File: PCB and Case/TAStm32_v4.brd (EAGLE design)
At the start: 50 x 100 mm, 37 parts, among them J1 ZX62D-B-5PA8, J10 RJSSE538002, J11 RJSSE538002, J12 SOICBITE, J13 CONSOLE_RESET, J2 UE27-AC54-100, J3 OLED128X64, J4 CONSOLE_RESET, J5 95278-802A12LF, J6 SAMTEC-TSM-106-01-X-SV_SAMTEC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, J7 SAMTEC-TSM-106-01-X-SV_SAMTEC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, J8 SAMTEC-TSM-106-01-X-SV_SAMTEC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, J9 SAMTEC-TSM-106-01-X-SV_SAMTEC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, U1 STM32F446RET6, U2 3.3V REG, Y1 8MHz

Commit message: 3D stuff
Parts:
- J10, J11: value RJSSE538002 -> RJSSE538002_RJSSE538002; device RJSSE538002:AMPHENOL_RJSSE538002 -> TAStm32_v4:AMPHENOL_RJSSE538002
- J13, J4: device TAStm32_v4:SAMTEC-TSM-102-01-X-SH_SAMTEC-TSM-102-01-X-SH -> TAStm32_v4:SAMTEC-TSM-102-01-X-SH
- J6, J7, J8, J9: value SAMTEC-TSM-106-01-X-SV_SAMTEC-TSM-106-01-X-SVJ -> SAMTEC-TSM-106-01-X-SV_SAMTEC-TSM-106-01-X-SV; device TAStm32_v4:SAMTEC-TSM-106-01-X-SV_SAMTEC-TSM-106-01-X-SV -> TAStm32_v4:SAMTEC-TSM-106-01-X-SV
- Y1: device TAStm32_v4:ABMM-8.000MHZ-B2-T_DFN-4 -> TAStm32_v4:DFN-4

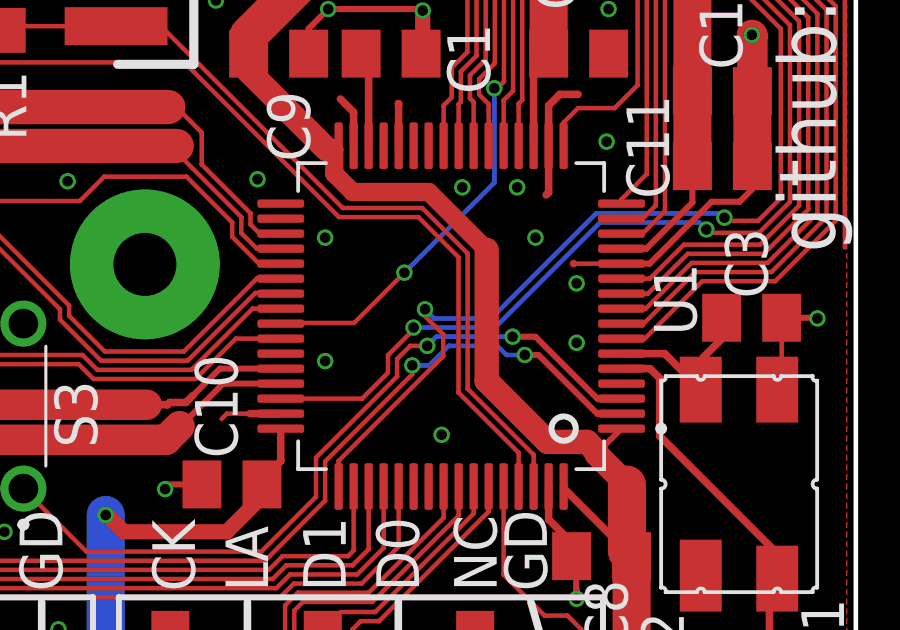
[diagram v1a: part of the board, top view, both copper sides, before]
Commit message: 3D packages
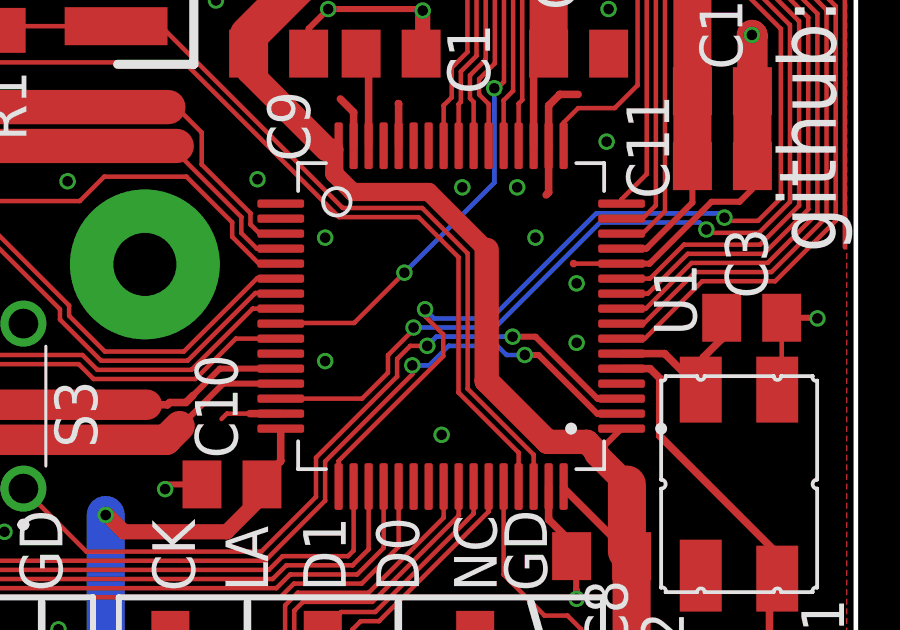
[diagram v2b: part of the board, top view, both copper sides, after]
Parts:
- U1: device TAStm32_v4:STM32F446RET6_QFP50P1200X1200X160-64N -> STM32F446RET6:QFP50P1200X1200X160-64N
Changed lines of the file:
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@@
 </layers>
 <board>
-<fusionsync huburn="a.cGVyc29uYWw6dWUyZjk5ODBk" projecturn="a.cGVyc29uYWw6dWUyZGI3NDIzIzIwMjAwNDAyMjgyMjQ0MjAx" f3durn="urn:adsk.wipprod:dm.lineage:3hYDGigSRSyFbyUFu3cILQ" pcbguid="358a8c1f-667c-482f-bf1c-2fc096c4186a" lastpulledtime="" lastsyncedchangeguid="38c33caf-a1b4-3c75-6ae5-50c6f9a0fab9"/>
+<fusionsync huburn="a.cGVyc29uYWw6dWUyZjk5ODBk" projecturn="a.cGVyc29uYWw6dWUyZGI3NDIzIzIwMjAwNDAyMjgyMjQ0MjAx" f3durn="urn:adsk.wipprod:dm.lineage:3hYDGigSRSyFbyUFu3cILQ" pcbguid="358a8c1f-667c-482f-bf1c-2fc096c4186a" lastpulledtime="" lastsyncedchangeguid="3421df81-c885-fb27-6cc6-82ec7bf5822e"/>
 <plain>
 <wire x1="0" y1="3" x2="0" y2="97" width="0.1524" layer="20"/>
@@
 <attribute name="VALUE" x="46.5508" y="45.9" size="1.016" layer="27" rot="R180"/>
 </element>
-<element name="U1" library="TAStm32_v4" package="STM32F446RET6_QFP50P1200X1200X160-64N" value="STM32F446RET6" x="36.508" y="36.5" smashed="yes" rot="R180">
-<attribute name="DESCRIPTION" value=" MCU 32-Bit STM32 ARM Cortex M4 RISC 512KB Flash 2.5V/3.3V 64-Pin LQFP Tray " x="36.508" y="36.5" size="1.778" layer="27" rot="R180" display="off"/>
-<attribute name="DIGI-KEY_PART_NUMBER" value="" x="36.508" y="36.5" size="1.778" layer="27" rot="R180" display="off"/>
-<attribute name="DIGI-KEY_PURCHASE_URL" value="" x="36.508" y="36.5" size="1.778" layer="27" rot="R180" display="off"/>
-<attribute name="MF" value="STMicroelectronics" x="36.508" y="36.5" size="1.778" layer="27" rot="R180" display="off"/>
-<attribute name="MP" value="STM32F446RET6" x="36.508" y="36.5" size="1.778" layer="27" rot="R180" display="off"/>
+<element name="U1" library="STM32F446RET6" package="QFP50P1200X1200X160-64N" package3d_urn="urn:adsk.eagle:package:18856813/2" value="STM32F446RET6" x="36.508" y="36.5" smashed="yes" rot="R180">
 <attribute name="NAME" x="43.26733125" y="38.258659375" size="1.4224" layer="25" font="vector" ratio="15" rot="R270"/>
-<attribute name="PACKAGE" value="LQFP-64 STMicroelectronics" x="36.508" y="36.5" size="1.778" layer="27" rot="R180" display="off"/>
 <attribute name="VALUE" x="43.0162" y="45.01071875" size="1.2716" layer="27" rot="R180"/>
 </element>

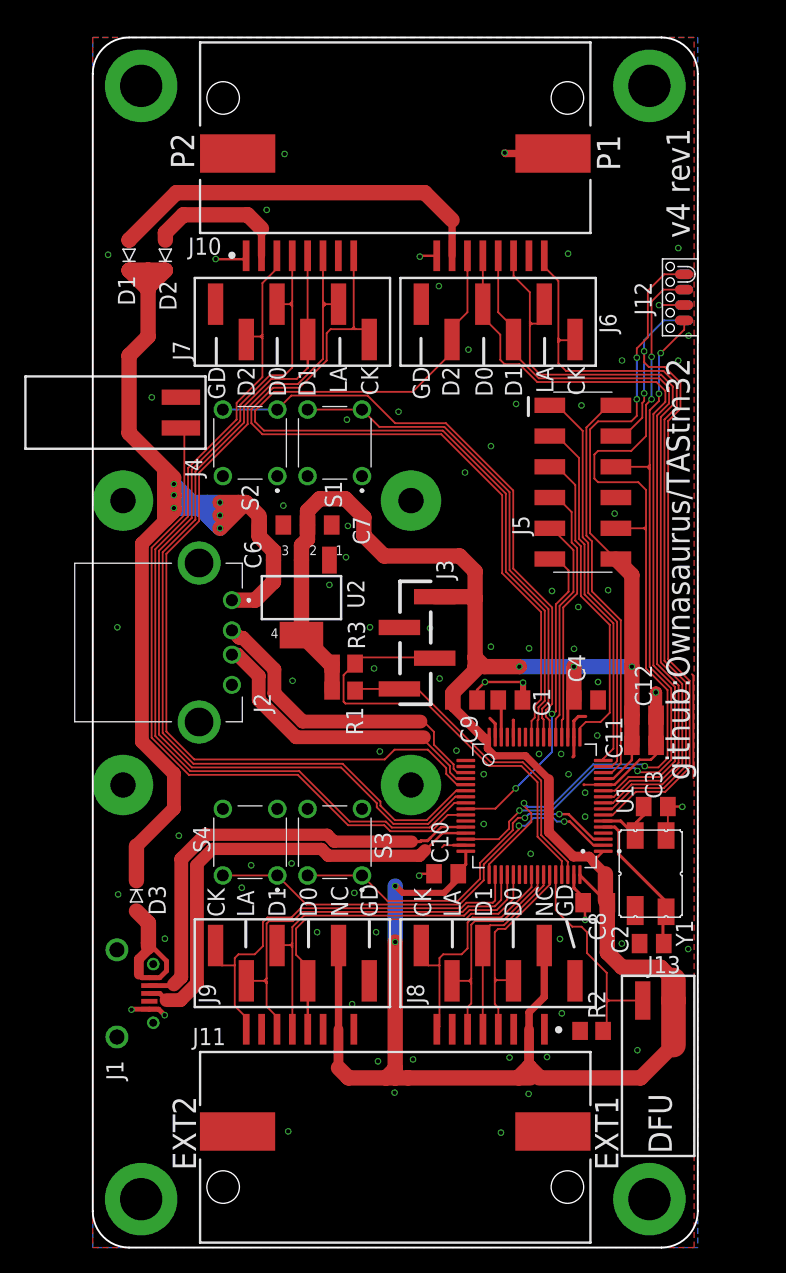
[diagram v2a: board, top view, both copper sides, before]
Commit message: Started adding level translators
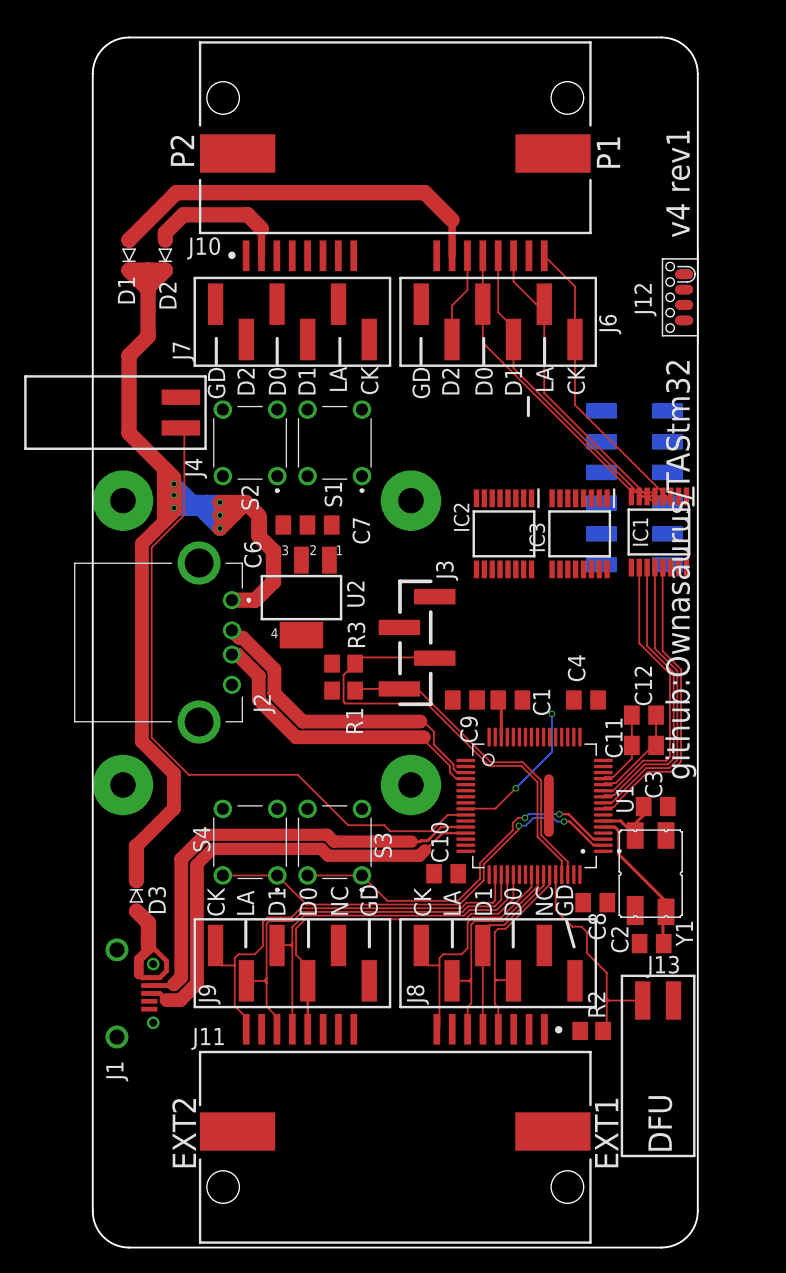
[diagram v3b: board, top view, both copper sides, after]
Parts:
- added IC1, IC2, IC3: 74AVCH4T245PW,118, SamacSys_Parts:SOP65P640X110-16N
- moved J5 4.29 mm to (44.8, 62.8), flipped to the bottom, turned to 270 degrees
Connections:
- new net N$11: IC2.6
- new net N$9: IC2.4
- new net P1_CLOCK_3V: IC1.13, U1.8
- new net P1_D0_3V: IC1.10, IC3.13, U1.11
- new net P1_D1_3V: IC1.11, IC3.12, U1.10
- new net P1_D2_3V: IC2.11, IC2.13, U1.24
- new net P1_D2_DIR: IC2.2
- new net P1_LATCH_3V: IC1.12, U1.9
- new net P2_CLOCK_3V: U1.25
- new net P2_D0_3V: IC3.11, U1.39
- new net P2_D1_3V: IC3.10, U1.38
- new net P2_D2_3V: U1.40
- new net P2_D2_DIR: IC2.3
- new net P2_LATCH_3V: U1.37
- new net PORTS_ENABLE: IC1.14, IC1.15, IC2.14, IC2.15, IC3.14, IC3.15
- net GND: now also IC1.3, IC1.8, IC1.9, IC2.8, IC2.9, IC3.2, IC3.3, IC3.8, IC3.9
- net P1_5V: now also IC1.1, IC1.2, IC2.1, IC3.1
- net P1_CLOCK: now also IC1.4; no longer U1.8
- net P1_D0: now also IC1.7, IC3.4; no longer U1.11
- net P1_D1: now also IC1.6, IC3.5; no longer U1.10
- net P1_D2: no longer U1.24
- net P1_LATCH: now also IC1.5; no longer U1.9
- net P2_CLOCK: no longer U1.25
- net P2_D0: now also IC3.6; no longer U1.39
- net P2_D1: now also IC3.7; no longer U1.38
- net P2_D2: no longer U1.40
- net P2_LATCH: no longer U1.37
- net V+: now also IC1.16, IC2.16, IC3.16
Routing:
- net V+: track 244.5 -> 11.0 mm, vias 7 -> 0
- net P2_D0: track 76.2 -> 0.00 mm
- net P2_LATCH: track 75.4 -> 0.00 mm
- net P2_D2: track 75.4 -> 0.00 mm
- net P2_D1: track 74.9 -> 0.00 mm
- net SWCLK: track 73.2 -> 0.00 mm, vias 4 -> 0
- net P2_CLOCK: track 67.0 -> 0.00 mm
- net P1_D2: track 73.3 -> 7.45 mm
- net SWDIO: track 62.0 -> 0.00 mm, vias 4 -> 0
- net NRST: track 59.6 -> 0.00 mm, vias 2 -> 0
- net GND: track 60.5 -> 8.21 mm, vias 85 -> 0
- net N$4: track 49.8 -> 0.00 mm
- net N$6: track 41.4 -> 0.00 mm
- net P1_CLOCK: track 62.7 -> 24.4 mm
- net P1_LATCH: track 65.3 -> 28.2 mm
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- removed copper zone on layer 1, net GND
- removed copper zone on layer 16, net GND

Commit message: different level translators
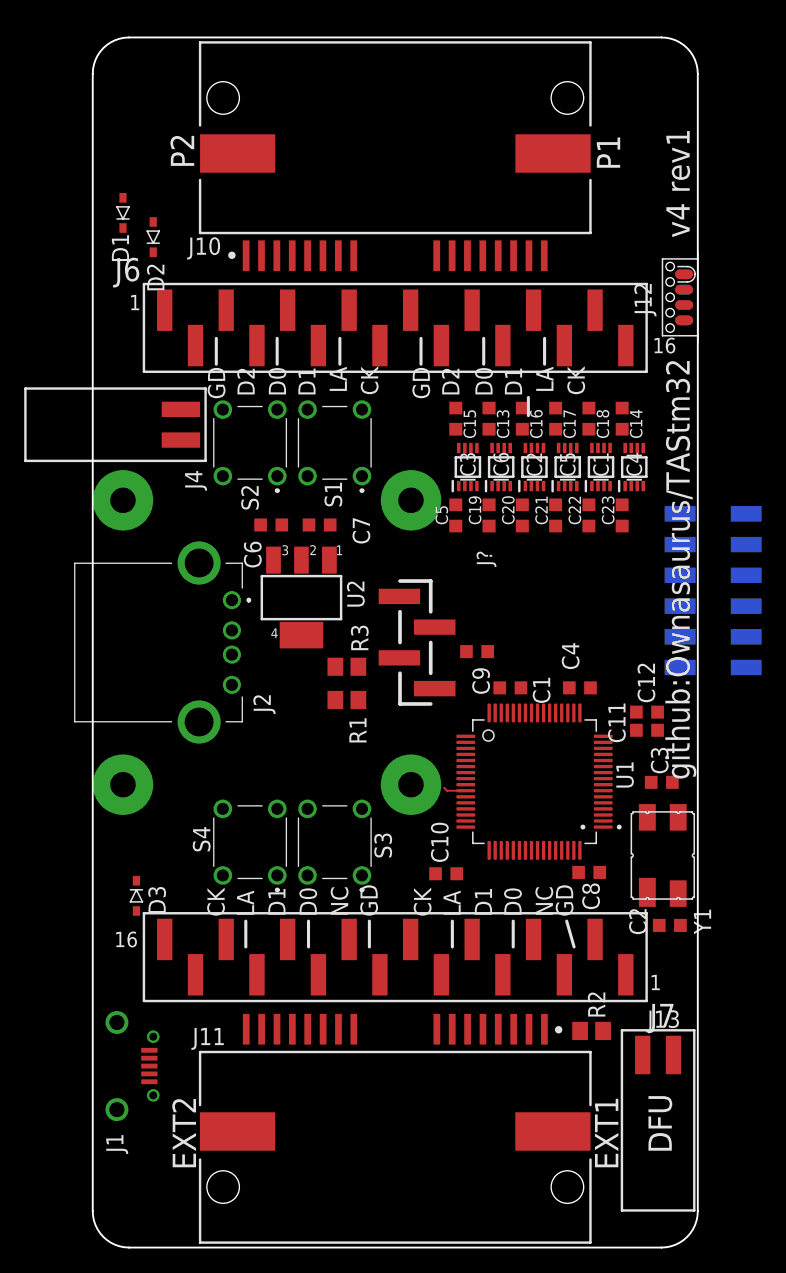
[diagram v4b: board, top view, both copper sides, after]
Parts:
- removed J3: OLED128X64, TAStm32_v4:OLED
- removed J8, J9: SAMTEC-TSM-106-01-X-SV_SAMTEC-TSM-106-01-X-SV, TAStm32_v4:SAMTEC-TSM-106-01-X-SV
- added C13, C14, C15, C16, C17, C18, C19, C20, C21, C22, C23, C5: 100nF, rcl:C0603K
- added IC4, IC5, IC6: 74LVCH2T45DC,125, SamacSys_Parts:SOP50P310X100-8N
- added J?: OLED128X64, TAStm32_v4:OLED
- C1, C10, C11, C12, C2, C3, C4, C6, C7, C8, C9: device rcl:C0805K -> rcl:C0603K
- IC1, IC2, IC3: value 74AVCH4T245PW,118 -> 74LVCH2T45DC,125; device SamacSys_Parts:SOP65P640X110-16N -> SamacSys_Parts:SOP50P310X100-8N
- J10, J11: value RJSSE538002_RJSSE538002 -> RJSSE538002
- J6, J7: value SAMTEC-TSM-106-01-X-SV_SAMTEC-TSM-106-01-X-SV -> SAMTEC-TSM-116-01-X-SVJ; device TAStm32_v4:SAMTEC-TSM-106-01-X-SV -> SAMTEC-TSM-116-01-X-SV:SAMTEC-TSM-116-01-X-SV
- moved J7 53.2 mm to (25.0, 24.0)
- moved IC3 10.8 mm to (31.0, 64.5), turned to 90 degrees
- moved J5 10.7 mm to (51.3, 54.3)
- moved J6 8.51 mm to (25.0, 76.0), turned to 0 degrees
- moved IC1 7.19 mm to (42.0, 64.5), turned to 90 degrees
- moved IC2 6.07 mm to (36.5, 64.5), turned to 90 degrees
- moved J1 6.00 mm to (2.00, 15.0)
- moved J13 4.50 mm to (46.7, 10.6)
- moved C9 4.12 mm to (31.8, 49.2)
- moved D1 3.54 mm to (2.50, 85.5)
- moved C8 2.55 mm to (41.0, 31.0)
- moved C2 2.12 mm to (47.7, 26.6)
- moved C3 2.06 mm to (47.0, 38.4)
- moved U1 2.00 mm to (36.5, 38.5)
- moved D2 1.80 mm to (5.00, 83.5)
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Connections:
- removed net N$11: IC2.6
- removed net P1_D2_DIR: IC2.2
- removed net P1_NC: J10.15
- removed net P2_D2_DIR: IC2.3
- removed net P2_NC: J10.7
- removed net PORTS_ENABLE: IC1.14, IC1.15, IC2.14, IC2.15, IC3.14, IC3.15
- new net DIR_D0D1: IC1.5, IC3.5
- new net DIR_P1D2D3: IC5.5
- new net DIR_P2D2D3: IC6.5
- new net N$8: IC5.3
- new net P1_D3: IC5.6, J10.15, J6.15
- new net P1_D3_3V: IC5.2
- new net P2_D3: IC6.6, J10.7, J6.7
- new net P2_D3_3V: IC6.2
- net GND: now also C13.1, C14.1, C15.1, C16.1, C17.1, C18.1, C19.1, C20.1, C21.1, C22.1, C23.1, C5.1, IC1.4, IC2.4, IC3.4, IC4.4, IC5.4, IC6.4, J6.1, J6.9, J7.1, J7.9, J?.1, J?.5, J?.6, J?.7, J?.8; no longer IC1.3, IC1.8, IC1.9, IC2.8, IC2.9, IC3.2, IC3.3, IC3.8, IC3.9, J3.2, J3.5, J3.6, J3.7, J3.8, J6.6, J7.6, J8.6, J9.6
- net I2C_SCL: now also J?.2; no longer J3.3
- net I2C_SDA: now also J?.3; no longer J3.4
- net N$9: now also IC6.3; no longer IC2.4
- net P1_5V: now also C13.2, C14.2, C15.2, C16.2, C17.2, IC1.8, IC2.8, IC3.8, IC4.8, IC5.8, J6.10; no longer IC1.1, IC1.2, IC2.1, IC3.1
- net P1_CLOCK: now also IC4.6, J6.16; no longer IC1.4, J6.1
- net P1_CLOCK_3V: now also IC4.3; no longer IC1.13
- net P1_D0: now also J6.12; no longer IC3.4, J6.4
- net P1_D0_3V: now also IC1.2; no longer IC1.10, IC3.13
- net P1_D1: now also J6.13; no longer IC3.5, J6.3
- net P1_D1_3V: now also IC1.3; no longer IC1.11, IC3.12
- net P1_D2: now also IC5.7, J6.11; no longer J6.5
- net P1_D2_3V: no longer IC2.11, IC2.13
- net P1_LATCH: now also IC4.7, J6.14; no longer IC1.5, J6.2
- net P1_LATCH_3V: now also IC4.2; no longer IC1.12
- net P2_5V: now also C18.2, IC6.8, J6.2
- net P2_CLOCK: now also IC2.6, J6.8; no longer J7.1
- net P2_CLOCK_3V: now also IC2.3
- net P2_D0: now also IC3.7, J6.4; no longer IC3.6, J7.4
- net P2_D0_3V: now also IC3.2; no longer IC3.11
- net P2_D1: now also IC3.6, J6.5; no longer IC3.7, J7.3
- net P2_D1_3V: now also IC3.3; no longer IC3.10
- net P2_D2: now also IC6.7, J6.3; no longer J7.5
- net P2_LATCH: now also IC2.7, J6.6; no longer J7.2
- net P2_LATCH_3V: now also IC2.2
- net V+: now also C19.2, C20.2, C21.2, C22.2, C23.2, C5.2, IC1.1, IC2.1, IC2.5, IC3.1, IC4.1, IC4.5, IC5.1, IC6.1, J7.10, J7.2, J?.4; no longer IC1.16, IC2.16, IC3.16, J3.1, J8.5, J9.5
- net V1_CLOCK: now also J7.8; no longer J8.1
- net V1_D0: now also J7.4; no longer J8.4
- net V1_D1: now also J7.5; no longer J8.3
- net V1_LATCH: now also J7.6; no longer J8.2
- net V1_NC: now also J7.7
- net V1_NC2: now also J7.3
- net V2_CLOCK: now also J7.16; no longer J9.1
- net V2_D0: now also J7.12; no longer J9.4
- net V2_D1: now also J7.13; no longer J9.3
- net V2_LATCH: now also J7.14; no longer J9.2
- net V2_NC: now also J7.15
- net V2_NC2: now also J7.11
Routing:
- net +5V: track 99.3 -> 0.00 mm, vias 6 -> 0
- net SNES_RESET: track 56.6 -> 1.90 mm
- net DP: track 38.4 -> 0.00 mm
- net DM: track 37.8 -> 0.00 mm
- net I2C_SCL: track 37.6 -> 0.00 mm
- net N$2: track 37.3 -> 0.00 mm, vias 2 -> 0
- net V2_CLOCK: track 36.0 -> 0.00 mm
- net V2_LATCH: track 33.7 -> 0.00 mm
- net P1_5V: track 32.2 -> 0.00 mm
- net V2_D1: track 30.9 -> 0.00 mm
- net N$3: track 30.2 -> 0.00 mm, vias 2 -> 0
- net V2_D0: track 29.9 -> 0.00 mm
- net P1_LATCH: track 28.2 -> 0.00 mm
- net P1_D0: track 27.9 -> 0.00 mm
- net I2C_SDA: track 27.3 -> 0.00 mm
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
